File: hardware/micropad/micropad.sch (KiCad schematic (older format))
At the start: 17 parts

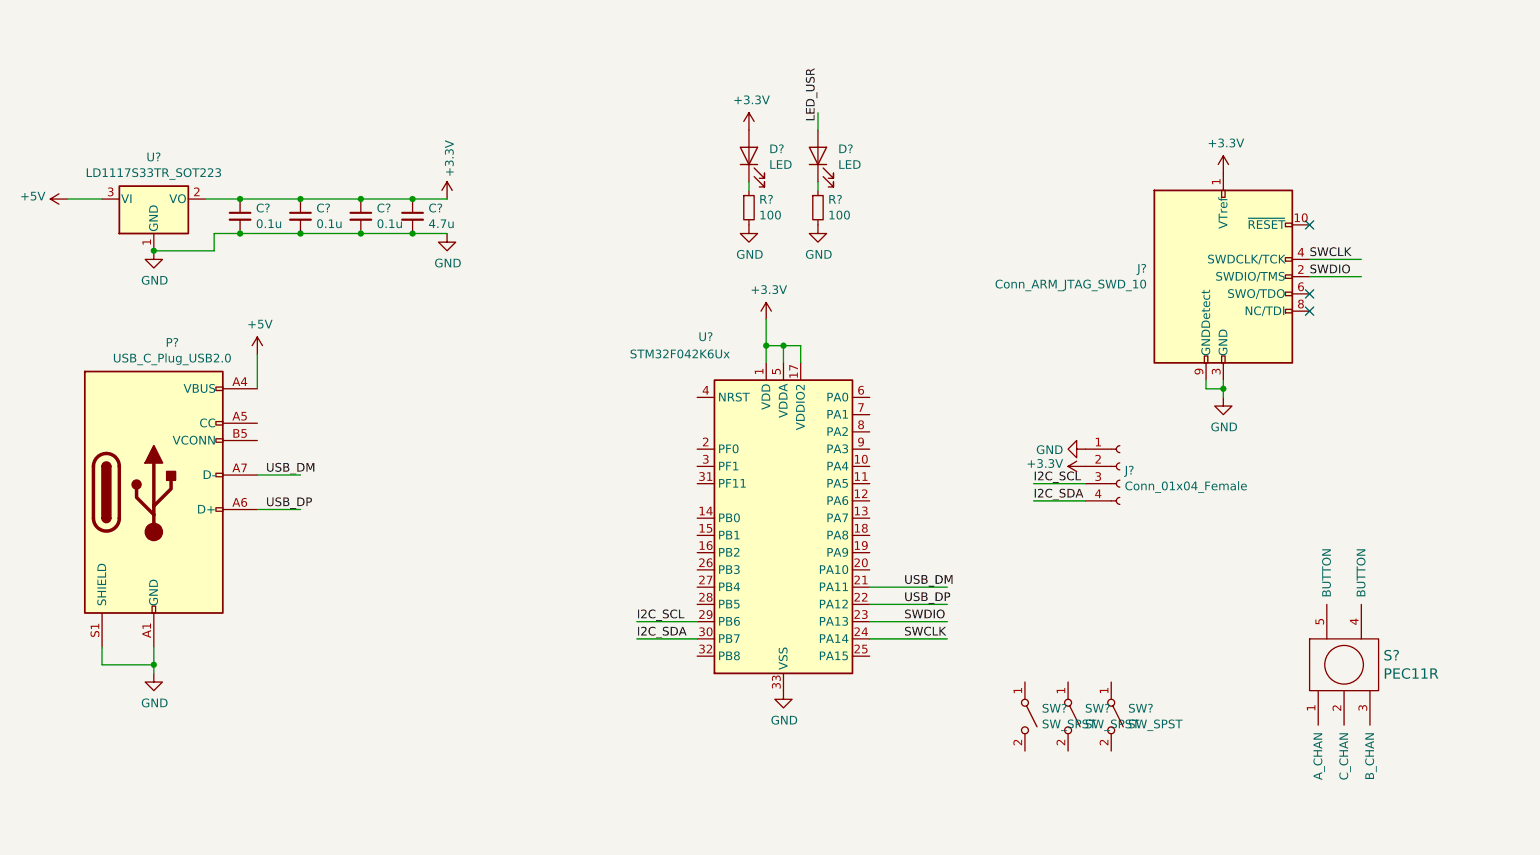
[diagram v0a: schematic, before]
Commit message: Continue connecting peripherals to the microcontroller
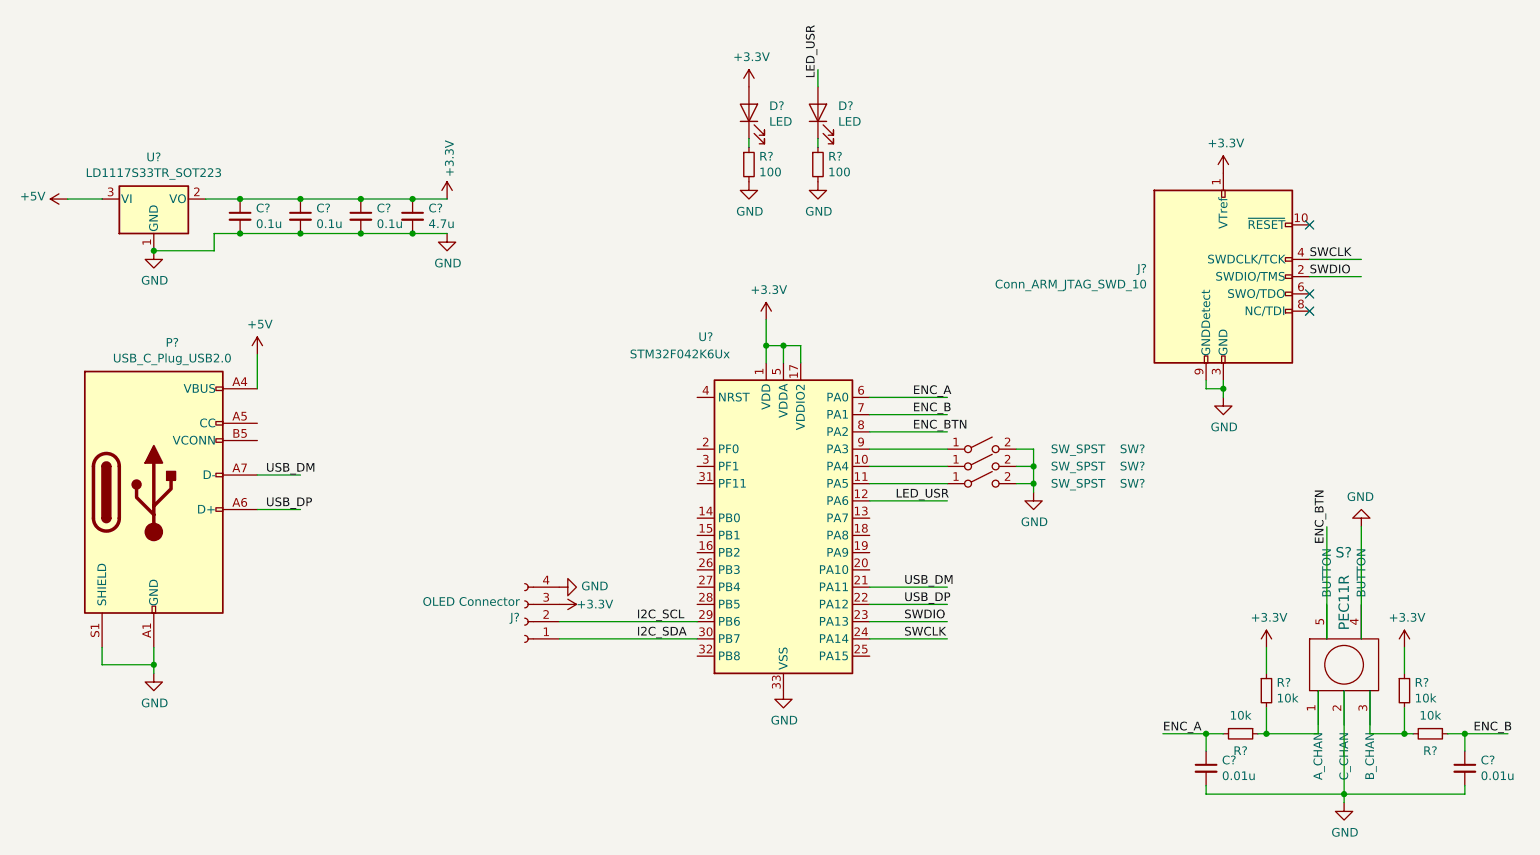
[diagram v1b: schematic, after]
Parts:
- added C? (x2): 0.01u, symbol Device:C_Small
- added R? (x4): 10k, symbol Device:R_Small
- J?: value Conn_01x04_Female -> OLED Connector
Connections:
- net labels added: ENC_A, ENC_B, ENC_BTN
- wire segments 43 -> 78
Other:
- moved on the sheet: D?, J?, R?, SW?

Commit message: Add USB footprint
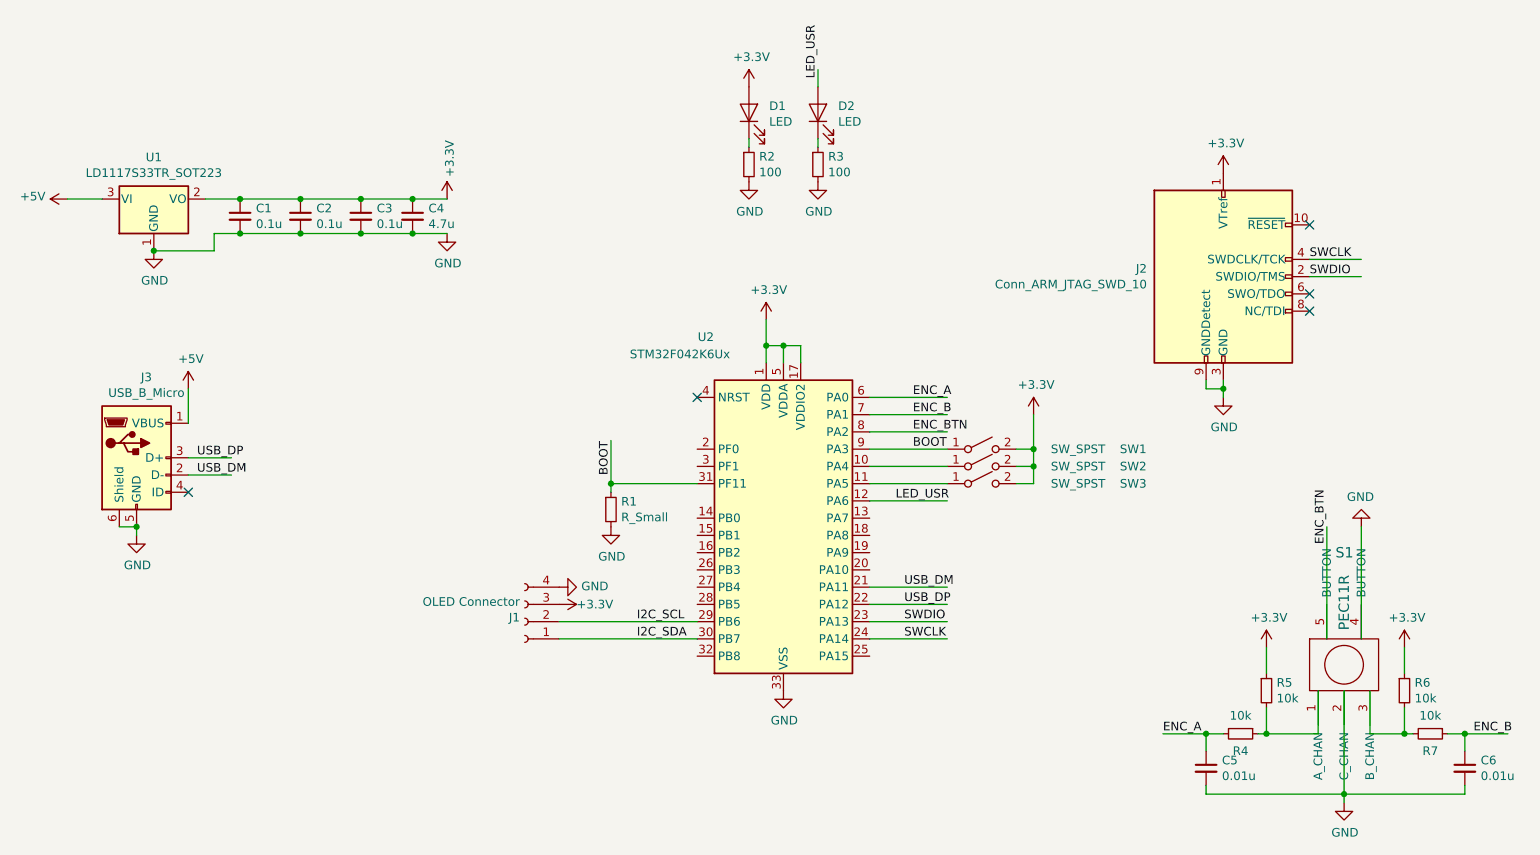
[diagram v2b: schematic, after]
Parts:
- removed P?: USB_C_Plug_USB2.0, symbol Connector:USB_C_Plug_USB2.0
- added J3: USB_B_Micro, micropad:XKB-U254_USB, symbol Connector:USB_B_Micro
- added R1: R_Small, Resistors_SMD:R_0805, symbol Device:R_Small
- C1, C2, C3, C4, C5, C6: renamed from C?; footprint (none) -> Capacitors_SMD:C_0805
- D1, D2: renamed from D?; footprint (none) -> LEDs:LED_0805
- J1: renamed from J?; footprint (none) -> Pin_Headers:Pin_Header_Straight_1x04_Pitch2.54mm
- J2: renamed from J?; footprint (none) -> Pin_Headers:Pin_Header_Straight_2x05_Pitch1.27mm_SMD
- R2, R3, R4, R5, R6, R7: renamed from R?; footprint (none) -> Resistors_SMD:R_0805
- S1: renamed from S?; footprint (none) -> micropad:PEC11
- SW1: renamed from SW?; footprint (none) -> Buttons_Switches_Keyboard:SW_Cherry_MX1A_2.00u_Plate
- SW2, SW3: renamed from SW?; footprint (none) -> Buttons_Switches_Keyboard:SW_Cherry_MX1A_1.00u_Plate
- gave numbers to parts that had none: 2
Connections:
- net labels added: BOOT
- wire segments 78 -> 79
- no-connect marks 3 -> 5

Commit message: Get PCB footprints to load
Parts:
- R1: value R_Small -> 10k
- U1: footprint Package_TO_SOT_SMD:SOT-223-3_TabPin2 -> TO_SOT_Packages_SMD:SOT-223-3_TabPin2
- U2: footprint Package_DFN_QFN:QFN-32-1EP_5x5mm_P0.5mm_EP3.45x3.45mm -> Housings_DFN_QFN:WQFN-32-1EP_5x5mm_Pitch0.5mm
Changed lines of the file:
@@
 F 0 "U2" H 5200 5100 50  0000 C CNN
 F 1 "STM32F042K6Ux" H 5050 5000 50  0000 C CNN
-F 2 "Package_DFN_QFN:QFN-32-1EP_5x5mm_P0.5mm_EP3.45x3.45mm" H 5250 3150 50  0001 R CNN
+F 2 "Housings_DFN_QFN:WQFN-32-1EP_5x5mm_Pitch0.5mm" H 5250 3150 50  0001 R CNN
 F 3 "http://www.st.com/st-web-ui/static/active/en/resource/technical/document/datasheet/DM00105814.pdf" H 5650 4050 50  0001 C CNN
 	1    5650 4050
@@
 F 0 "U1" H 2000 2442 50  0000 C CNN
 F 1 "LD1117S33TR_SOT223" H 2000 2351 50  0000 C CNN
-F 2 "Package_TO_SOT_SMD:SOT-223-3_TabPin2" H 2000 2400 50  0001 C CNN
+F 2 "TO_SOT_Packages_SMD:SOT-223-3_TabPin2" H 2000 2400 50  0001 C CNN
 F 3 "http://www.st.com/st-web-ui/static/active/en/resource/technical/document/datasheet/CD00000544.pdf" H 2100 1950 50  0001 C CNN
 	1    2000 2200
@@
 P 4650 4000
 F 0 "R1" H 4709 4046 50  0000 L CNN
-F 1 "R_Small" H 4709 3955 50  0000 L CNN
+F 1 "10k" H 4709 3955 50  0000 L CNN
 F 2 "Resistors_SMD:R_0805" H 4650 4000 50  0001 C CNN
 F 3 "~" H 4650 4000 50  0001 C CNN
